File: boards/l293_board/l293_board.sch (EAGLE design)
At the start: 7 parts, among them IC1 L293D

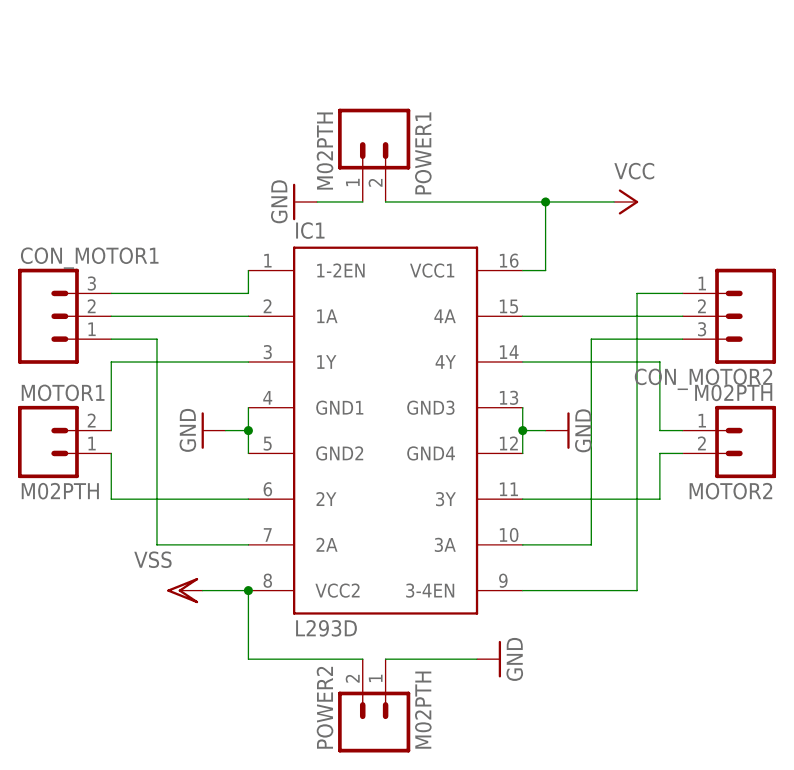
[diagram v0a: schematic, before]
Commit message: updated board to make 5x2 connector
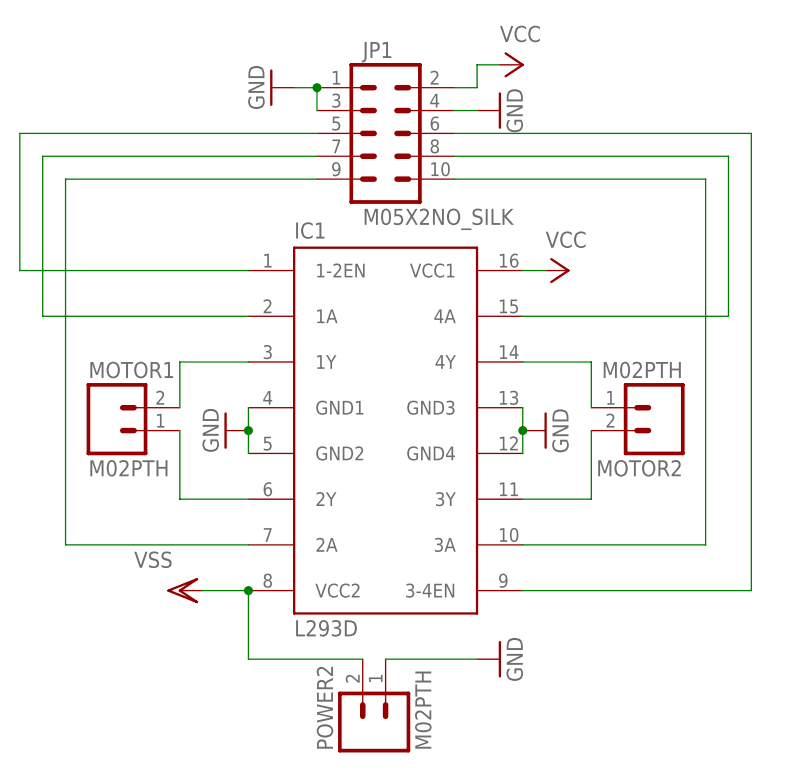
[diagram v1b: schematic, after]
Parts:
- removed CON_MOTOR1, CON_MOTOR2: (no value), SparkFun-Connectors:M03PTH
- removed POWER1: M02PTH, SparkFun-Connectors:M02PTH
- added JP1: M05X2NO_SILK, SparkFun-Connectors:M05X2NO_SILK
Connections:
- net GND: now also JP1.1, JP1.3, JP1.4; no longer POWER1.1
- net N$1: now also JP1.6; no longer CON_MOTOR2.1
- net N$11: now also JP1.10; no longer CON_MOTOR2.3
- net N$2: now also JP1.5; no longer CON_MOTOR1.3
- net N$5: now also JP1.8; no longer CON_MOTOR2.2
- net N$6: now also JP1.7; no longer CON_MOTOR1.2
- net N$7: now also JP1.9; no longer CON_MOTOR1.1
- net VCC: now also JP1.2; no longer POWER1.2
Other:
- moved on the sheet: MOTOR1, MOTOR2
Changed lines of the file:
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@@
 <classes>
 <class number="0" name="default" width="0" drill="0">
+<clearance class="0" value="0.205"/>
 </class>
 </classes>
@@
 <part name="POWER2" library="SparkFun-Connectors" deviceset="M02" device="PTH"/>
 <part name="GND4" library="supply1" deviceset="GND" device=""/>
-<part name="GND5" library="supply1" deviceset="GND" device=""/>
 <part name="P+3" library="supply1" deviceset="VCC" device=""/>
-<part name="CON_MOTOR1" library="SparkFun-Connectors" deviceset="M03" device="PTH"/>
-<part name="CON_MOTOR2" library="SparkFun-Connectors" deviceset="M03" device="PTH"/>
-<part name="POWER1" library="SparkFun-Connectors" deviceset="M02" device="PTH"/>
+<part name="JP1" library="SparkFun-Connectors" deviceset="M05X2" device="NO_SILK"/>
+<part name="P+1" library="supply1" deviceset="VCC" device=""/>
+<part name="GND1" library="supply1" deviceset="GND" device=""/>
+<part name="GND6" library="supply1" deviceset="GND" device=""/>
 </parts>
 <sheets>
@@
 <instance part="IC1" gate="G$1" x="0" y="0"/>
 <instance part="VSS1" gate="G$1" x="-22.86" y="-17.78" rot="R270"/>
-<instance part="GND2" gate="1" x="-20.32" y="0" rot="R270"/>
-<instance part="GND3" gate="1" x="20.32" y="0" rot="R90"/>
-<instance part="MOTOR2" gate="G$1" x="40.64" y="0" rot="R180"/>
-<instance part="MOTOR1" gate="G$1" x="-38.1" y="-2.54"/>
+<instance part="GND2" gate="1" x="-17.78" y="0" rot="R270"/>
+<instance part="GND3" gate="1" x="17.78" y="0" rot="R90"/>
+<instance part="MOTOR2" gate="G$1" x="30.48" y="2.54" rot="R180"/>
+<instance part="MOTOR1" gate="G$1" x="-30.48" y="0"/>
 <instance part="POWER2" gate="G$1" x="0" y="-33.02" rot="R90"/>
 <instance part="GND4" gate="1" x="12.7" y="-25.4" rot="R90"/>
-<instance part="GND5" gate="1" x="-10.16" y="25.4" rot="R270"/>
-<instance part="P+3" gate="VCC" x="27.94" y="25.4" rot="R270"/>
-<instance part="CON_MOTOR1" gate="G$1" x="-38.1" y="12.7"/>
-<instance part="CON_MOTOR2" gate="G$1" x="40.64" y="12.7" rot="R180"/>
-<instance part="POWER1" gate="G$1" x="-2.54" y="33.02" rot="R270"/>
+<instance part="P+3" gate="VCC" x="20.32" y="17.78" rot="R270"/>
+<instance part="JP1" gate="G$1" x="0" y="33.02"/>
+<instance part="P+1" gate="VCC" x="15.24" y="40.64" rot="R270"/>
+<instance part="GND1" gate="1" x="-12.7" y="38.1" rot="R270"/>
+<instance part="GND6" gate="1" x="12.7" y="35.56" rot="R90"/>
 </instances>
 <busses>
@@
 <pinref part="GND2" gate="1" pin="GND"/>
 <wire x1="-15.24" y1="0" x2="-15.24" y2="-2.54" width="0.1524" layer="91"/>
-<wire x1="-17.78" y1="0" x2="-15.24" y2="0" width="0.1524" layer="91"/>
 <junction x="-15.24" y="0"/>
 </segment>
@@
 <pinref part="GND3" gate="1" pin="GND"/>
 <wire x1="15.24" y1="0" x2="15.24" y2="-2.54" width="0.1524" layer="91"/>
-<wire x1="17.78" y1="0" x2="15.24" y2="0" width="0.1524" layer="91"/>
 <junction x="15.24" y="0"/>
 </segment>
@@
 </segment>
 <segment>
-<pinref part="GND5" gate="1" pin="GND"/>
-<pinref part="POWER1" gate="G$1" pin="1"/>
-<wire x1="-7.62" y1="25.4" x2="-2.54" y2="25.4" width="0.1524" layer="91"/>
+<pinref part="GND6" gate="1" pin="GND"/>
+<pinref part="JP1" gate="G$1" pin="4"/>
+<wire x1="10.16" y1="35.56" x2="7.62" y2="35.56" width="0.1524" layer="91"/>
+</segment>
+<segment>
+<pinref part="GND1" gate="1" pin="GND"/>
+<pinref part="JP1" gate="G$1" pin="1"/>
+<wire x1="-10.16" y1="38.1" x2="-7.62" y2="38.1" width="0.1524" layer="91"/>
+<pinref part="JP1" gate="G$1" pin="3"/>
+<wire x1="-7.62" y1="35.56" x2="-7.62" y2="38.1" width="0.1524" layer="91"/>
+<junction x="-7.62" y="38.1"/>
 </segment>
 </net>
@@
 <segment>
 <pinref part="IC1" gate="G$1" pin="1Y"/>
-<wire x1="-15.24" y1="7.62" x2="-30.48" y2="7.62" width="0.1524" layer="91"/>
-<wire x1="-30.48" y1="7.62" x2="-30.48" y2="0" width="0.1524" layer="91"/>
+<wire x1="-15.24" y1="7.62" x2="-22.86" y2="7.62" width="0.1524" layer="91"/>
+<wire x1="-22.86" y1="7.62" x2="-22.86" y2="2.54" width="0.1524" layer="91"/>
 <pinref part="MOTOR1" gate="G$1" pin="2"/>
 </segment>
@@
 <segment>
 <pinref part="IC1" gate="G$1" pin="2Y"/>
-<wire x1="-15.24" y1="-7.62" x2="-30.48" y2="-7.62" width="0.1524" layer="91"/>
-<wire x1="-30.48" y1="-7.62" x2="-30.48" y2="-2.54" width="0.1524" layer="91"/>
+<wire x1="-15.24" y1="-7.62" x2="-22.86" y2="-7.62" width="0.1524" layer="91"/>
+<wire x1="-22.86" y1="-7.62" x2="-22.86" y2="0" width="0.1524" layer="91"/>
 <pinref part="MOTOR1" gate="G$1" pin="1"/>
 </segment>
@@
 <segment>
 <pinref part="IC1" gate="G$1" pin="4Y"/>
-<wire x1="15.24" y1="7.62" x2="30.48" y2="7.62" width="0.1524" layer="91"/>
-<wire x1="30.48" y1="7.62" x2="30.48" y2="0" width="0.1524" layer="91"/>
+<wire x1="15.24" y1="7.62" x2="22.86" y2="7.62" width="0.1524" layer="91"/>
+<wire x1="22.86" y1="7.62" x2="22.86" y2="2.54" width="0.1524" layer="91"/>
 <pinref part="MOTOR2" gate="G$1" pin="1"/>
-<wire x1="30.48" y1="0" x2="33.02" y2="0" width="0.1524" layer="91"/>
 </segment>
 </net>
@@
 <segment>
 <pinref part="MOTOR2" gate="G$1" pin="2"/>
-<wire x1="33.02" y1="-2.54" x2="30.48" y2="-2.54" width="0.1524" layer="91"/>
-<wire x1="30.48" y1="-2.54" x2="30.48" y2="-7.62" width="0.1524" layer="91"/>
+<wire x1="22.86" y1="0" x2="22.86" y2="-7.62" width="0.1524" layer="91"/>
 <pinref part="IC1" gate="G$1" pin="3Y"/>
-<wire x1="30.48" y1="-7.62" x2="15.24" y2="-7.62" width="0.1524" layer="91"/>
+<wire x1="22.86" y1="-7.62" x2="15.24" y2="-7.62" width="0.1524" layer="91"/>
 </segment>
 </net>
@@
 <segment>
 <pinref part="IC1" gate="G$1" pin="3-4EN"/>
-<wire x1="15.24" y1="-17.78" x2="27.94" y2="-17.78" width="0.1524" layer="91"/>
-<pinref part="CON_MOTOR2" gate="G$1" pin="1"/>
-<wire x1="33.02" y1="15.24" x2="27.94" y2="15.24" width="0.1524" layer="91"/>
-<wire x1="27.94" y1="15.24" x2="27.94" y2="-17.78" width="0.1524" layer="91"/>
+<wire x1="15.24" y1="-17.78" x2="40.64" y2="-17.78" width="0.1524" layer="91"/>
+<wire x1="40.64" y1="33.02" x2="40.64" y2="-17.78" width="0.1524" layer="91"/>
+<pinref part="JP1" gate="G$1" pin="6"/>
+<wire x1="7.62" y1="33.02" x2="40.64" y2="33.02" width="0.1524" layer="91"/>
 </segment>
 </net>
@@
 <segment>
 <pinref part="IC1" gate="G$1" pin="4A"/>
-<pinref part="CON_MOTOR2" gate="G$1" pin="2"/>
-<wire x1="33.02" y1="12.7" x2="15.24" y2="12.7" width="0.1524" layer="91"/>
+<wire x1="38.1" y1="12.7" x2="15.24" y2="12.7" width="0.1524" layer="91"/>
+<wire x1="38.1" y1="30.48" x2="38.1" y2="12.7" width="0.1524" layer="91"/>
+<pinref part="JP1" gate="G$1" pin="8"/>
+<wire x1="7.62" y1="30.48" x2="38.1" y2="30.48" width="0.1524" layer="91"/>
 </segment>
 </net>
 <net name="N$2" class="0">
 <segment>
-<pinref part="CON_MOTOR1" gate="G$1" pin="3"/>
 <pinref part="IC1" gate="G$1" pin="1-2EN"/>
-<wire x1="-30.48" y1="15.24" x2="-15.24" y2="15.24" width="0.1524" layer="91"/>
-<wire x1="-15.24" y1="15.24" x2="-15.24" y2="17.78" width="0.1524" layer="91"/>
+<wire x1="-40.64" y1="17.78" x2="-15.24" y2="17.78" width="0.1524" layer="91"/>
+<wire x1="-40.64" y1="33.02" x2="-40.64" y2="17.78" width="0.1524" layer="91"/>
+<pinref part="JP1" gate="G$1" pin="5"/>
+<wire x1="-40.64" y1="33.02" x2="-7.62" y2="33.02" width="0.1524" layer="91"/>
 </segment>
 </net>
 <net name="N$6" class="0">
 <segment>
-<pinref part="CON_MOTOR1" gate="G$1" pin="2"/>
 <pinref part="IC1" gate="G$1" pin="1A"/>
-<wire x1="-30.48" y1="12.7" x2="-15.24" y2="12.7" width="0.1524" layer="91"/>
+<wire x1="-38.1" y1="12.7" x2="-15.24" y2="12.7" width="0.1524" layer="91"/>
+<wire x1="-38.1" y1="30.48" x2="-38.1" y2="12.7" width="0.1524" layer="91"/>
+<pinref part="JP1" gate="G$1" pin="7"/>
+<wire x1="-38.1" y1="30.48" x2="-7.62" y2="30.48" width="0.1524" layer="91"/>
 </segment>
 </net>
 <net name="N$7" class="0">
 <segment>
-<pinref part="CON_MOTOR1" gate="G$1" pin="1"/>
-<wire x1="-30.48" y1="10.16" x2="-25.4" y2="10.16" width="0.1524" layer="91"/>
-<wire x1="-25.4" y1="10.16" x2="-25.4" y2="-12.7" width="0.1524" layer="91"/>
 <pinref part="IC1" gate="G$1" pin="2A"/>
-<wire x1="-25.4" y1="-12.7" x2="-15.24" y2="-12.7" width="0.1524" layer="91"/>
+<wire x1="-35.56" y1="27.94" x2="-35.56" y2="-12.7" width="0.1524" layer="91"/>
+<wire x1="-35.56" y1="-12.7" x2="-15.24" y2="-12.7" width="0.1524" layer="91"/>
+<pinref part="JP1" gate="G$1" pin="9"/>
+<wire x1="-35.56" y1="27.94" x2="-7.62" y2="27.94" width="0.1524" layer="91"/>
 </segment>
 </net>
 <net name="N$11" class="0">
 <segment>
-<pinref part="CON_MOTOR2" gate="G$1" pin="3"/>
-<wire x1="33.02" y1="10.16" x2="22.86" y2="10.16" width="0.1524" layer="91"/>
-<wire x1="22.86" y1="10.16" x2="22.86" y2="-12.7" width="0.1524" layer="91"/>
 <pinref part="IC1" gate="G$1" pin="3A"/>
-<wire x1="22.86" y1="-12.7" x2="15.24" y2="-12.7" width="0.1524" layer="91"/>
+<wire x1="35.56" y1="-12.7" x2="15.24" y2="-12.7" width="0.1524" layer="91"/>
+<wire x1="35.56" y1="27.94" x2="35.56" y2="-12.7" width="0.1524" layer="91"/>
+<pinref part="JP1" gate="G$1" pin="10"/>
+<wire x1="7.62" y1="27.94" x2="35.56" y2="27.94" width="0.1524" layer="91"/>
 </segment>
 </net>
 <net name="VCC" class="0">
 <segment>
+<pinref part="P+3" gate="VCC" pin="VCC"/>
 <pinref part="IC1" gate="G$1" pin="VCC1"/>
-<wire x1="17.78" y1="25.4" x2="17.78" y2="17.78" width="0.1524" layer="91"/>
 <wire x1="17.78" y1="17.78" x2="15.24" y2="17.78" width="0.1524" layer="91"/>
-<pinref part="POWER1" gate="G$1" pin="2"/>
-<wire x1="0" y1="25.4" x2="17.78" y2="25.4" width="0.1524" layer="91"/>
-<pinref part="P+3" gate="VCC" pin="VCC"/>
-<wire x1="17.78" y1="25.4" x2="25.4" y2="25.4" width="0.1524" layer="91"/>
-<junction x="17.78" y="25.4"/>
+</segment>
+<segment>
+<pinref part="JP1" gate="G$1" pin="2"/>
+<wire x1="7.62" y1="38.1" x2="10.16" y2="38.1" width="0.1524" layer="91"/>
+<wire x1="10.16" y1="38.1" x2="10.16" y2="40.64" width="0.1524" layer="91"/>
+<pinref part="P+1" gate="VCC" pin="VCC"/>
+<wire x1="10.16" y1="40.64" x2="12.7" y2="40.64" width="0.1524" layer="91"/>
 </segment>
 </net>
